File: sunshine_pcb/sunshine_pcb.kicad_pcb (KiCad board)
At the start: 4 copper layers, 30.5 x 44.7 mm, 46 parts, among them J2 Conn_01x04, J5 VerticalUSB, Q1 AO3400A, U1 ESP32-S3-WROOM-1, U2 SPX1117M3, U3 LIS3MDL, U4 ADXL375, U8 USBLC6-2P6

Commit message: Add voltage sense line
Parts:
- added D7: SMF5.0A, PCM_JLCPCB:D_SOD-123FL, B.Cu at (106.9, 109.9)
- added R14: 1kΩ, PCM_JLCPCB:R_0402, F.Cu at (105.2, 141.1)
- added R15: 1kΩ, PCM_JLCPCB:R_0402, F.Cu at (103.3, 141.1)
- added R9: 1kΩ, PCM_JLCPCB:R_0402, F.Cu at (107.2, 141.1)
- added VSENSE: VSENS, Connector_Wire:SolderWire-0.25sqmm_1x01_D0.65mm_OD1.7mm, F.Cu at (103.6, 110.6)
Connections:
- U1 pad 32: unconnected-(U1-IO39-Pad32) -> /VSENSE
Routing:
- net /VSE: track 0.00 -> 42.0 mm, vias 0 -> 6
- net GND: track 70.8 -> 73.5 mm, vias 67 -> 71
- net /VSENSE: track 0.00 -> 2.52 mm
- net Net-(R14-Pad2): track 0.00 -> 1.00 mm

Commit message: Use brighter LED
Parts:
- removed R13: 33Ω, PCM_JLCPCB:R_0805
- added R16: 27Ω, PCM_JLCPCB:R_0805, F.Cu at (104.5, 143.5)
- R10, R8: value 33Ω -> 27Ω
- R12: value 33Ω -> 27Ω; moved to B.Cu
- moved R10 2.00 mm to (104.5, 145.5)
- moved R12 2.00 mm to (104.5, 143.5)
- renumbered VSENSE to J1
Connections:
- R10 pad 2: Net-(D1-A) -> Net-(D4-A)
- R12 pad 2: Net-(D4-A) -> Net-(D5-A)

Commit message: Re-layout PCB
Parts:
- removed D7: SMF5.0A, PCM_JLCPCB:D_SOD-123FL
- removed R14, R9: 1kΩ, PCM_JLCPCB:R_0402
- added C1: 120u, Capacitor_THT:CP_Radial_D6.3mm_P2.50mm, F.Cu at (118.8, 91.4)
- added D11: H5VLD3B, PCM_JLCPCB:D_SOD-323, F.Cu at (78.5, 99.0)
- added J3: PWROUT, Connector_Wire:SolderWire-1.5sqmm_1x02_P6mm_D1.7mm_OD3mm, F.Cu at (80.8, 88.2)
- added R13: 2kΩ, PCM_JLCPCB:R_0402, F.Cu at (78.6, 97.0)
- added R17: 1kΩ, PCM_JLCPCB:R_0402, F.Cu at (80.4, 97.8)
- added SW1: SW_SPST, custom:screw_switch, F.Cu at (95.0, 91.2)
- C2: value 10u -> 120u; footprint Capacitor_SMD:C_1210_3225Metric -> Capacitor_THT:CP_Radial_D6.3mm_P2.50mm; moved to F.Cu
- C25, C26, C3, C4, C8, D2, D6, D8, R1, R12, R2, R20, R21, R3, R6, R7, R8, U4: moved to F.Cu
- D10, D9: value SMF5.0A -> H5VLD3B; footprint PCM_JLCPCB:D_SOD-123FL -> PCM_JLCPCB:D_SOD-323; moved to F.Cu
- D4: moved to B.Cu
- J1: value VSENS -> PWRIN; footprint Connector_Wire:SolderWire-0.25sqmm_1x01_D0.65mm_OD1.7mm -> Connector_AMASS:AMASS_XT30PW-M_1x02_P2.50mm_Horizontal
- moved R15 49.7 mm to (80.4, 97.0), turned to 0 degrees
- moved C6 33.2 mm to (106.2, 111.5), turned to -90 degrees
- moved C9 32.1 mm to (87.0, 137.9), turned to -90 degrees
- moved C8 31.4 mm to (87.9, 137.9), turned to -90 degrees
- moved C7 30.4 mm to (106.2, 145.7), turned to 0 degrees
- moved C27 30.1 mm to (97.6, 140.7)
- moved U3 30.0 mm to (94.2, 139.8), turned to 90 degrees
- moved C2 28.8 mm to (111.6, 91.3), turned to 90 degrees
- moved R2 28.3 mm to (115.7, 117.5), turned to 90 degrees
- moved C28 28.0 mm to (97.6, 139.8), turned to 0 degrees
- moved U2 27.7 mm to (100.8, 111.7), turned to 0 degrees
- moved S1 25.8 mm to (106.3, 142.4), turned to 90 degrees
- moved C29 25.5 mm to (97.6, 138.9), turned to 0 degrees
- moved R6 24.9 mm to (90.5, 140.3), turned to 180 degrees
- moved R21 24.6 mm to (90.1, 137.9), turned to -90 degrees
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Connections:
- C2 pad 1: /5V_IN -> /BATT+_IN
- C2 pad 2: GND -> /BATT-
- D10 pad 1: /S1_C -> GND
- D10 pad 2: GND -> /S1_C
- D9 pad 1: /S2_C -> GND
- D9 pad 2: GND -> /S2_C
- J1 pad 1: /VSE -> /BATT-
- R15 pad 1: /VSENSE -> /VSE
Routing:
- net +3V3: track 122.6 -> 1.41 mm, vias 11 -> 0
- net GND: track 73.5 -> 0.00 mm, vias 71 -> 0
- net /VSE: track 42.0 -> 0.00 mm, vias 6 -> 0
- net +5V: track 35.3 -> 0.00 mm, vias 3 -> 0
- net /MAG_DRDY: track 31.8 -> 0.00 mm, vias 2 -> 0
- net /EN: track 30.6 -> 0.00 mm, vias 2 -> 0
- net /MAG_INT: track 29.9 -> 0.00 mm, vias 2 -> 0
- net VBUS: track 29.2 -> 0.00 mm, vias 3 -> 0
- net /IMU_CS: track 25.6 -> 0.00 mm, vias 1 -> 0
- net /5V_IN: track 24.7 -> 0.00 mm
- net /IMU_MISO: track 24.3 -> 0.00 mm, vias 1 -> 0
- net /S1_C: track 23.9 -> 0.00 mm, vias 2 -> 0
- net /IMU_SCK: track 23.5 -> 0.00 mm, vias 1 -> 0
- net /BOOT: track 22.4 -> 0.00 mm, vias 2 -> 0
- net Net-(D1-K): track 21.2 -> 0.00 mm, vias 2 -> 0
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- removed copper zone on B.Cu, net /5V_IN
- removed copper zone on B.Cu, net GND
- removed copper zone on F.Cu, net GND
- removed copper zone on In1.Cu, net GND
- removed copper zone on In2.Cu, net GND
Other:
- board size 30.5 x 44.7 mm -> 45.5 x 66.7 mm
- board text added: "+ -"
- board text removed: "+5V"
- board text removed: "GND"
- board text removed: "S1"
- board text removed: "S2"

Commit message: Fix switch
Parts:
- moved R1 0.60 mm to (110.2, 114.4)
- moved R17 0.10 mm to (80.4, 97.9)
- turned C3 to -90 degrees
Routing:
- net +3V3: track 1.41 -> 96.0 mm, vias 0 -> 8
- net GND: track 0.00 -> 47.3 mm, vias 0 -> 27
- net /S2_C: track 0.00 -> 46.1 mm, vias 0 -> 2
- net /IMU_INT1: track 0.00 -> 45.8 mm, vias 0 -> 2
- net /IMU_CS: track 0.00 -> 45.2 mm, vias 0 -> 2
- net /IMU_INT2: track 0.00 -> 42.2 mm, vias 0 -> 2
- net +5V: track 0.00 -> 37.3 mm, vias 0 -> 2
- net /IMU_MISO: track 0.00 -> 35.6 mm, vias 0 -> 2
- net /IMU_MOSI: track 0.00 -> 35.4 mm, vias 0 -> 2
- net /IMU_SCK: track 0.00 -> 34.7 mm, vias 0 -> 2
- net /VSENSE: track 0.00 -> 34.3 mm, vias 0 -> 2
- net /S1_C: track 0.00 -> 33.6 mm, vias 0 -> 2
- net /5V_IN: track 0.00 -> 33.4 mm, vias 0 -> 2
- net /EN: track 0.00 -> 33.0 mm, vias 0 -> 4
- net /BOOT: track 0.00 -> 30.0 mm, vias 0 -> 3
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- added copper zone on F.Cu, net +3V3
- added copper zone on F.Cu, net +5V
- added copper zone on F.Cu, net /5V_IN
- added copper zone on B.Cu, net /BATT+
- added copper zone on F.Cu, net /BATT+
- added copper zone on B.Cu, net /BATT+_IN
- added copper zone on F.Cu, net /BATT+_IN
- added copper zone on In1.Cu, net /BATT-
- added copper zone on In2.Cu, net /BATT-
- added copper zone on B.Cu, net GND
- added copper zone on F.Cu, net GND
- added copper zone on In1.Cu, net GND
- added copper zone on In2.Cu, net GND
- added copper zone on B.Cu, net Net-(D1-K)
- added copper zone on F.Cu, net Net-(D1-K)

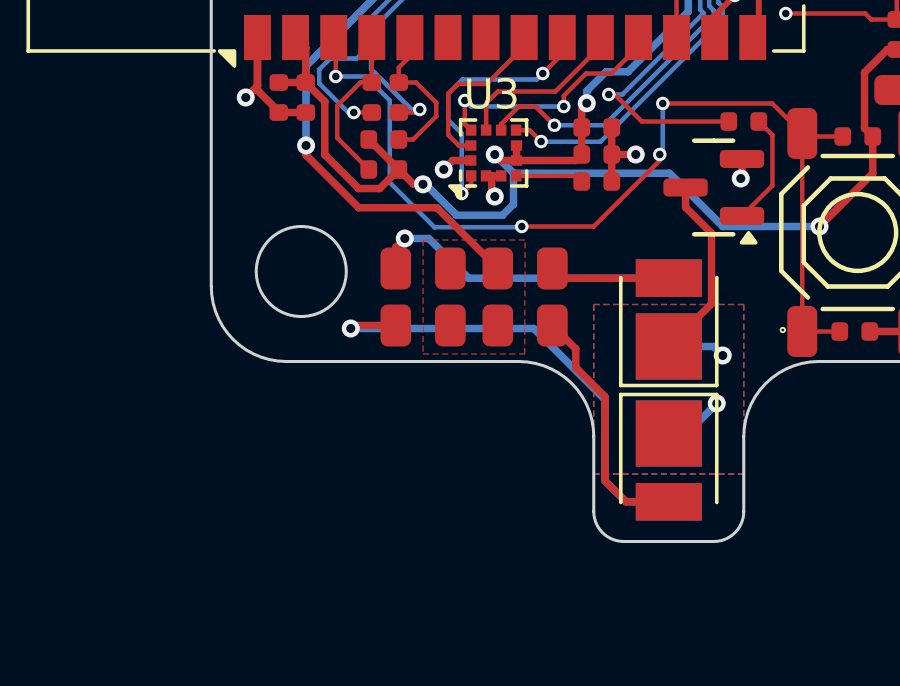
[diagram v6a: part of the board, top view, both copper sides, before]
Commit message: Fix hole clearance
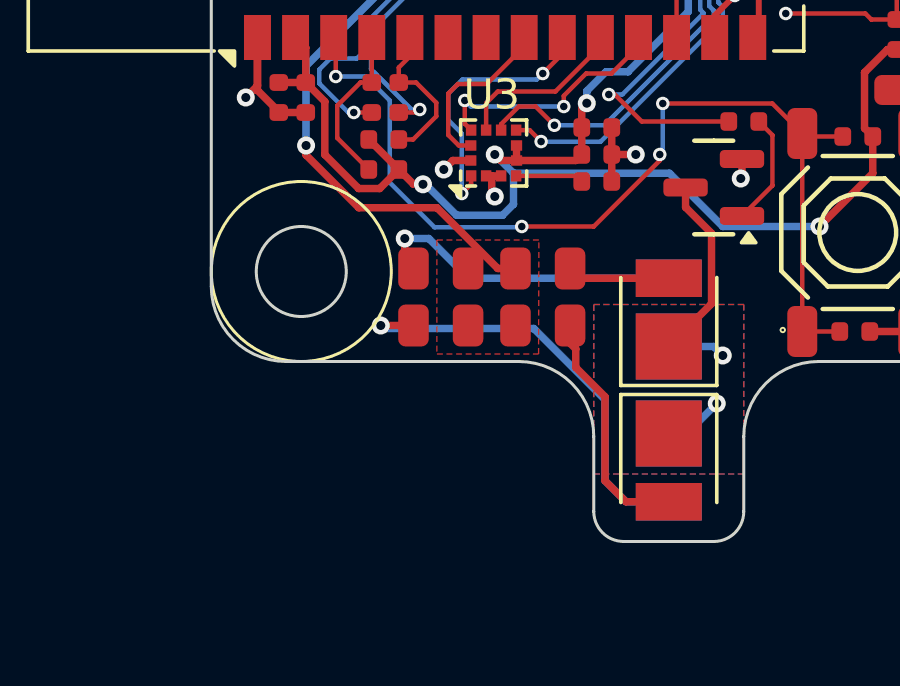
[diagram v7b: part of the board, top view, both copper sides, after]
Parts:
- moved R10 0.59 mm to (92.4, 143.6)
- moved R12 0.59 mm to (92.4, 145.5)
- moved R16 0.59 mm to (95.8, 143.6)
- moved R8 0.59 mm to (95.8, 145.5)
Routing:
- net Net-(D5-A): track 16.1 -> 14.7 mm
- net +5V: track 37.3 -> 37.9 mm
- net Net-(D4-A): track 10.5 -> 11.1 mm
